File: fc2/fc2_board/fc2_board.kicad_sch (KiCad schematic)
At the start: 5 parts, among them U1 MPU-6050, U2 STM32G070RBTx

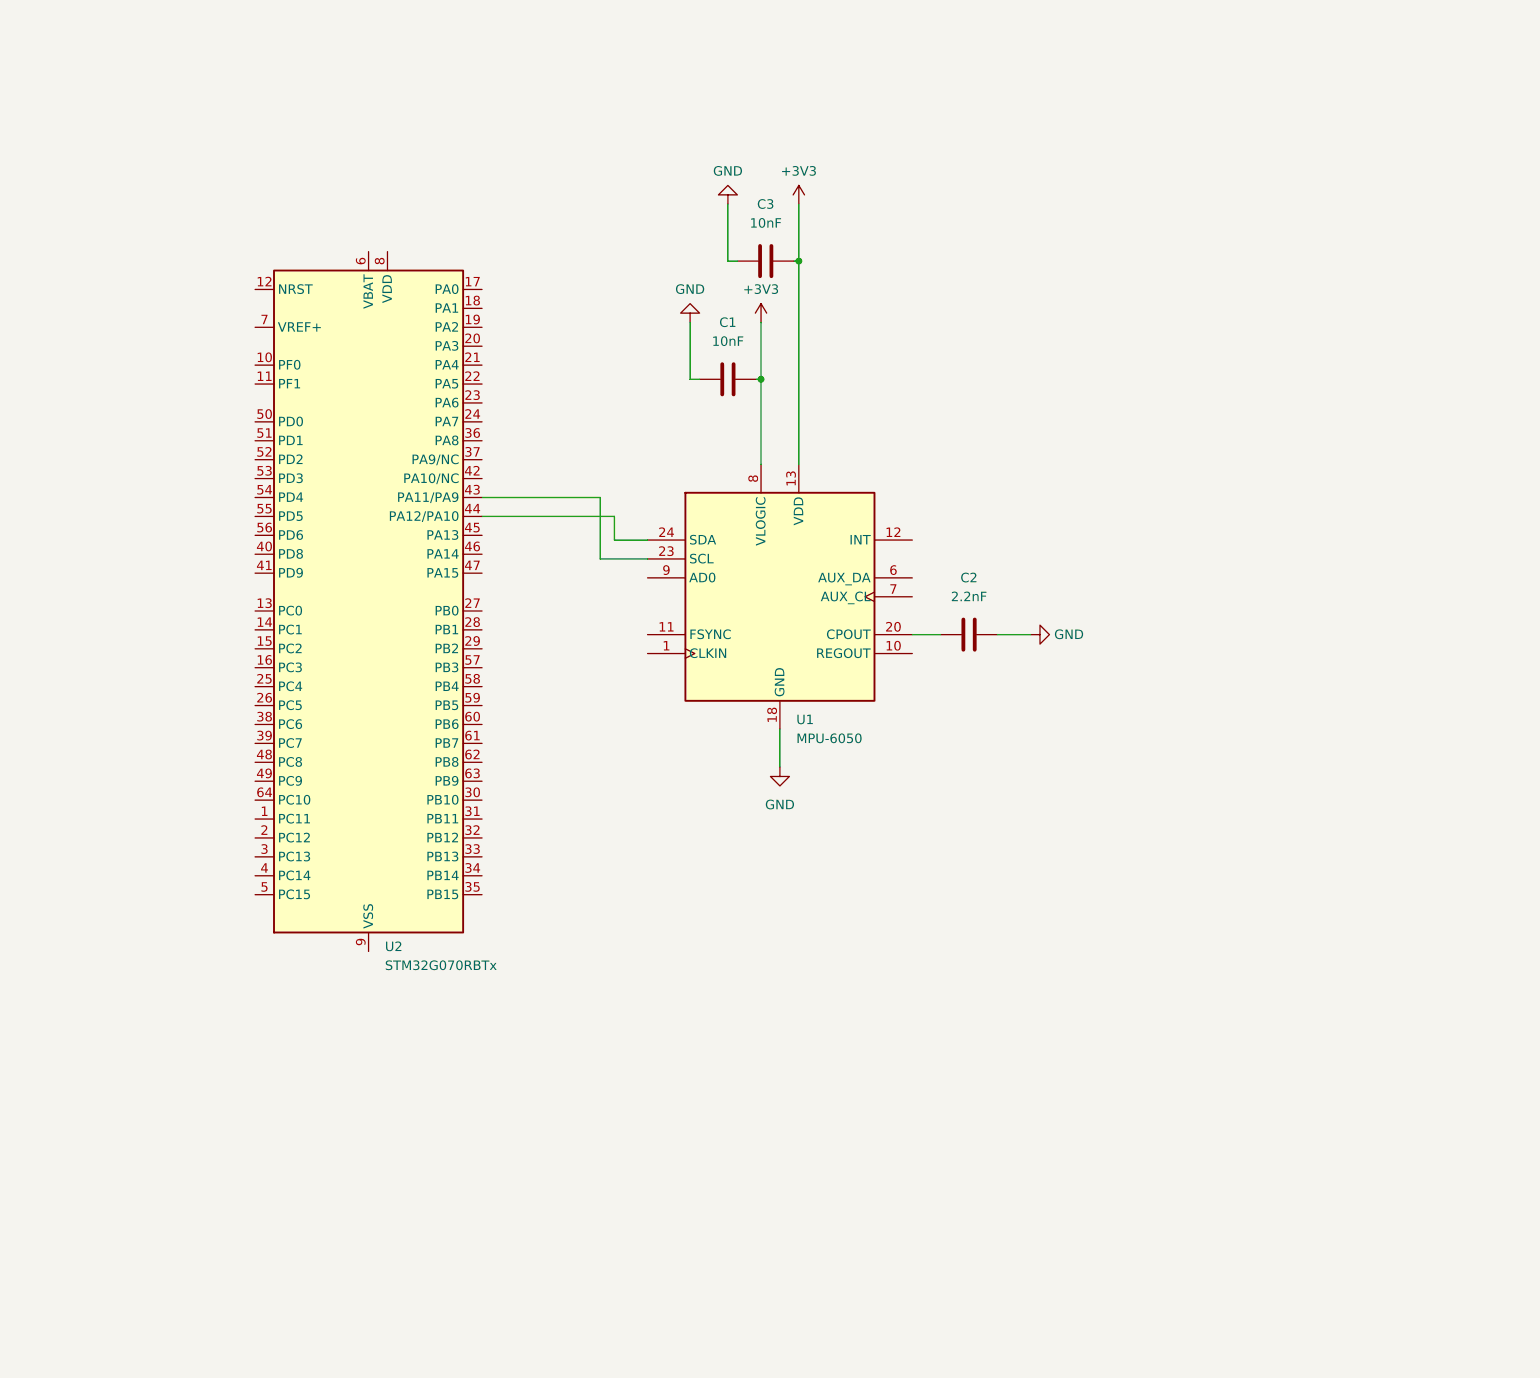
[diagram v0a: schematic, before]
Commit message: feat: add power on LED
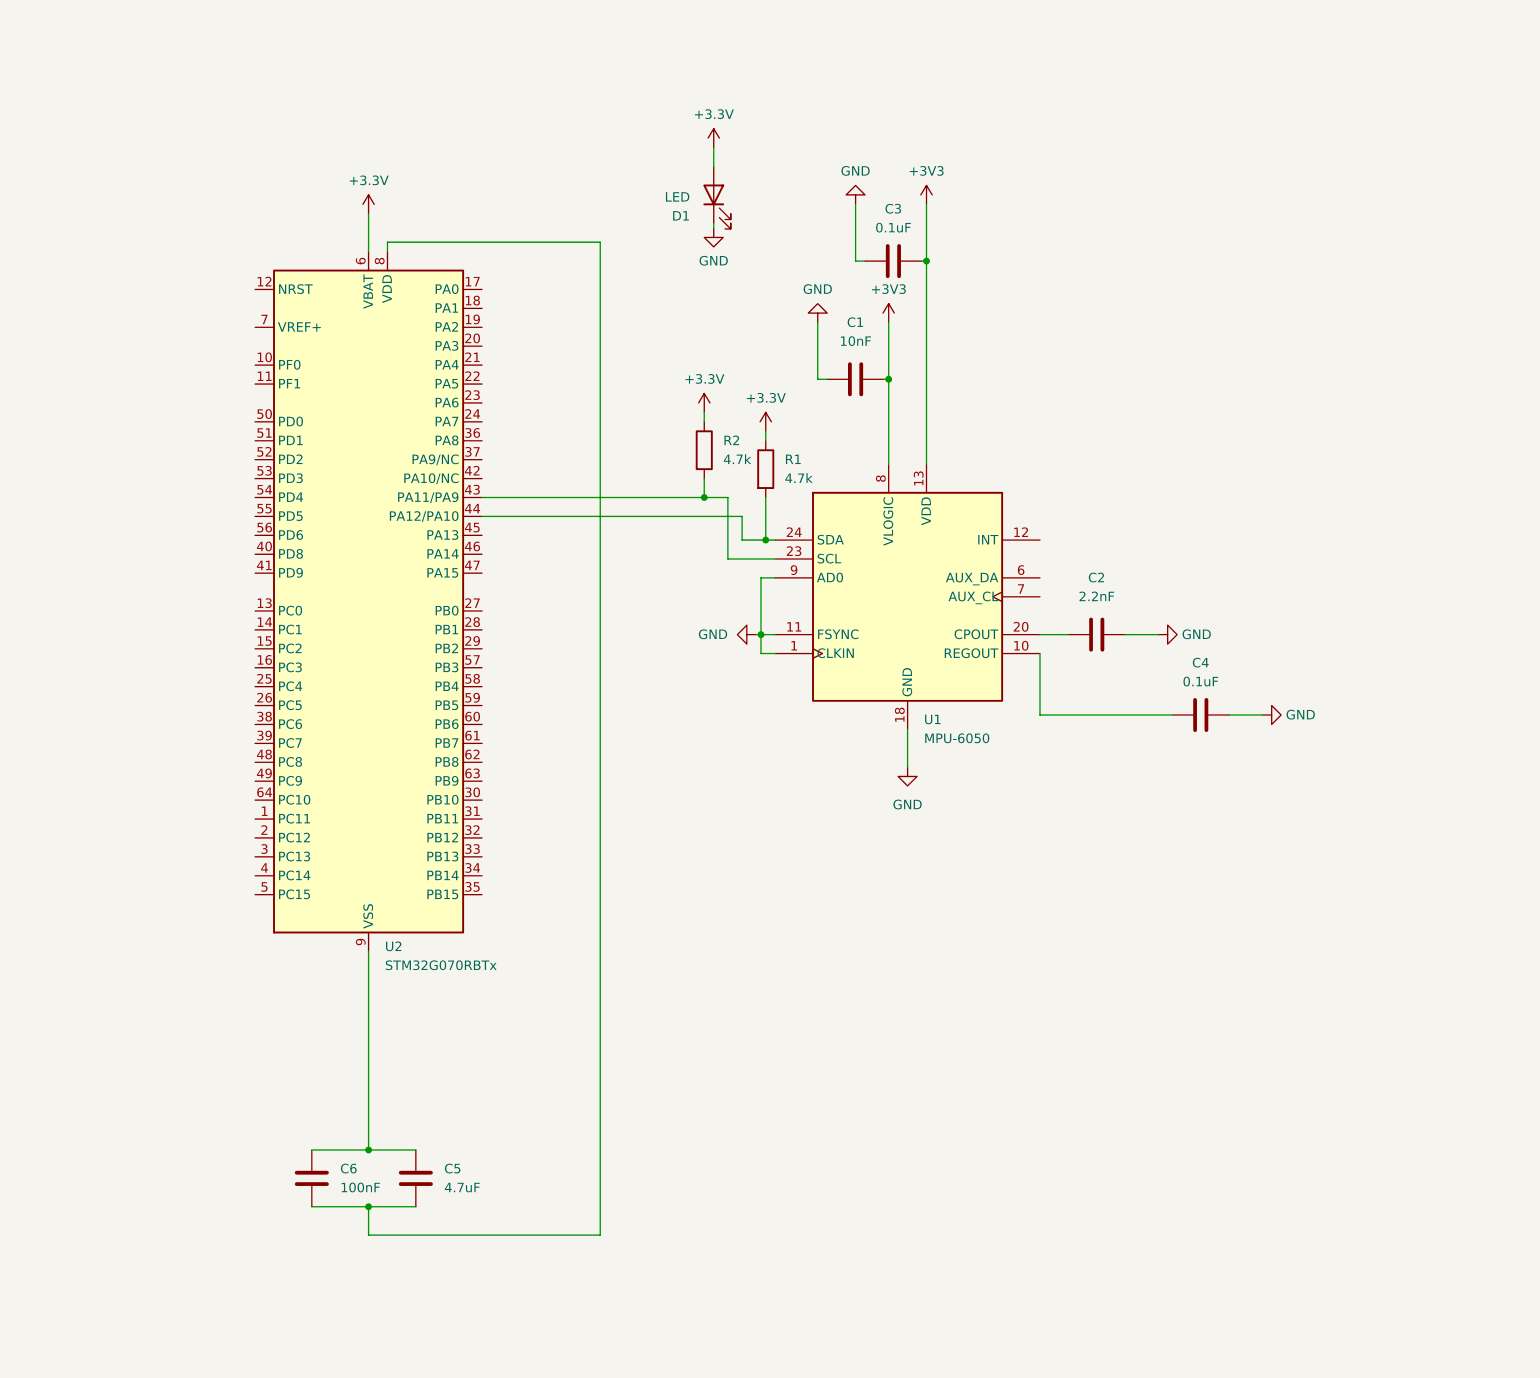
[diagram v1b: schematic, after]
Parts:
- added C4: 0.1uF, symbol Device:C
- added C5: 4.7uF, symbol Device:C
- added C6: 100nF, symbol Device:C
- added D1: LED, symbol Device:LED
- added R1, R2: 4.7k, symbol Device:R
- C3: value 10nF -> 0.1uF
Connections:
- net GND: now also U1.1 (CLKIN), U1.11 (FSYNC), U1.9 (AD0), C4.2, D1.1 (K)
- net at U1.10 (REGOUT): now also C4.1
- net at U1.23 (SCL), U2.43 (PA11/PA9): now also R2.2
- net at U1.24 (SDA), U2.44 (PA12/PA10): now also R1.2
- net +3.3V: now reaches U2.6 (VBAT)
- net +3.3V: now also D1.2 (A), R1.1, R2.1
- net at U2.8 (VDD): now also C5.2, C6.2
- net at U2.9 (VSS): now also C5.1, C6.1
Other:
- moved on the sheet: C1, C2, C3, U1

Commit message: kicad: add SAM-m10q to fc2
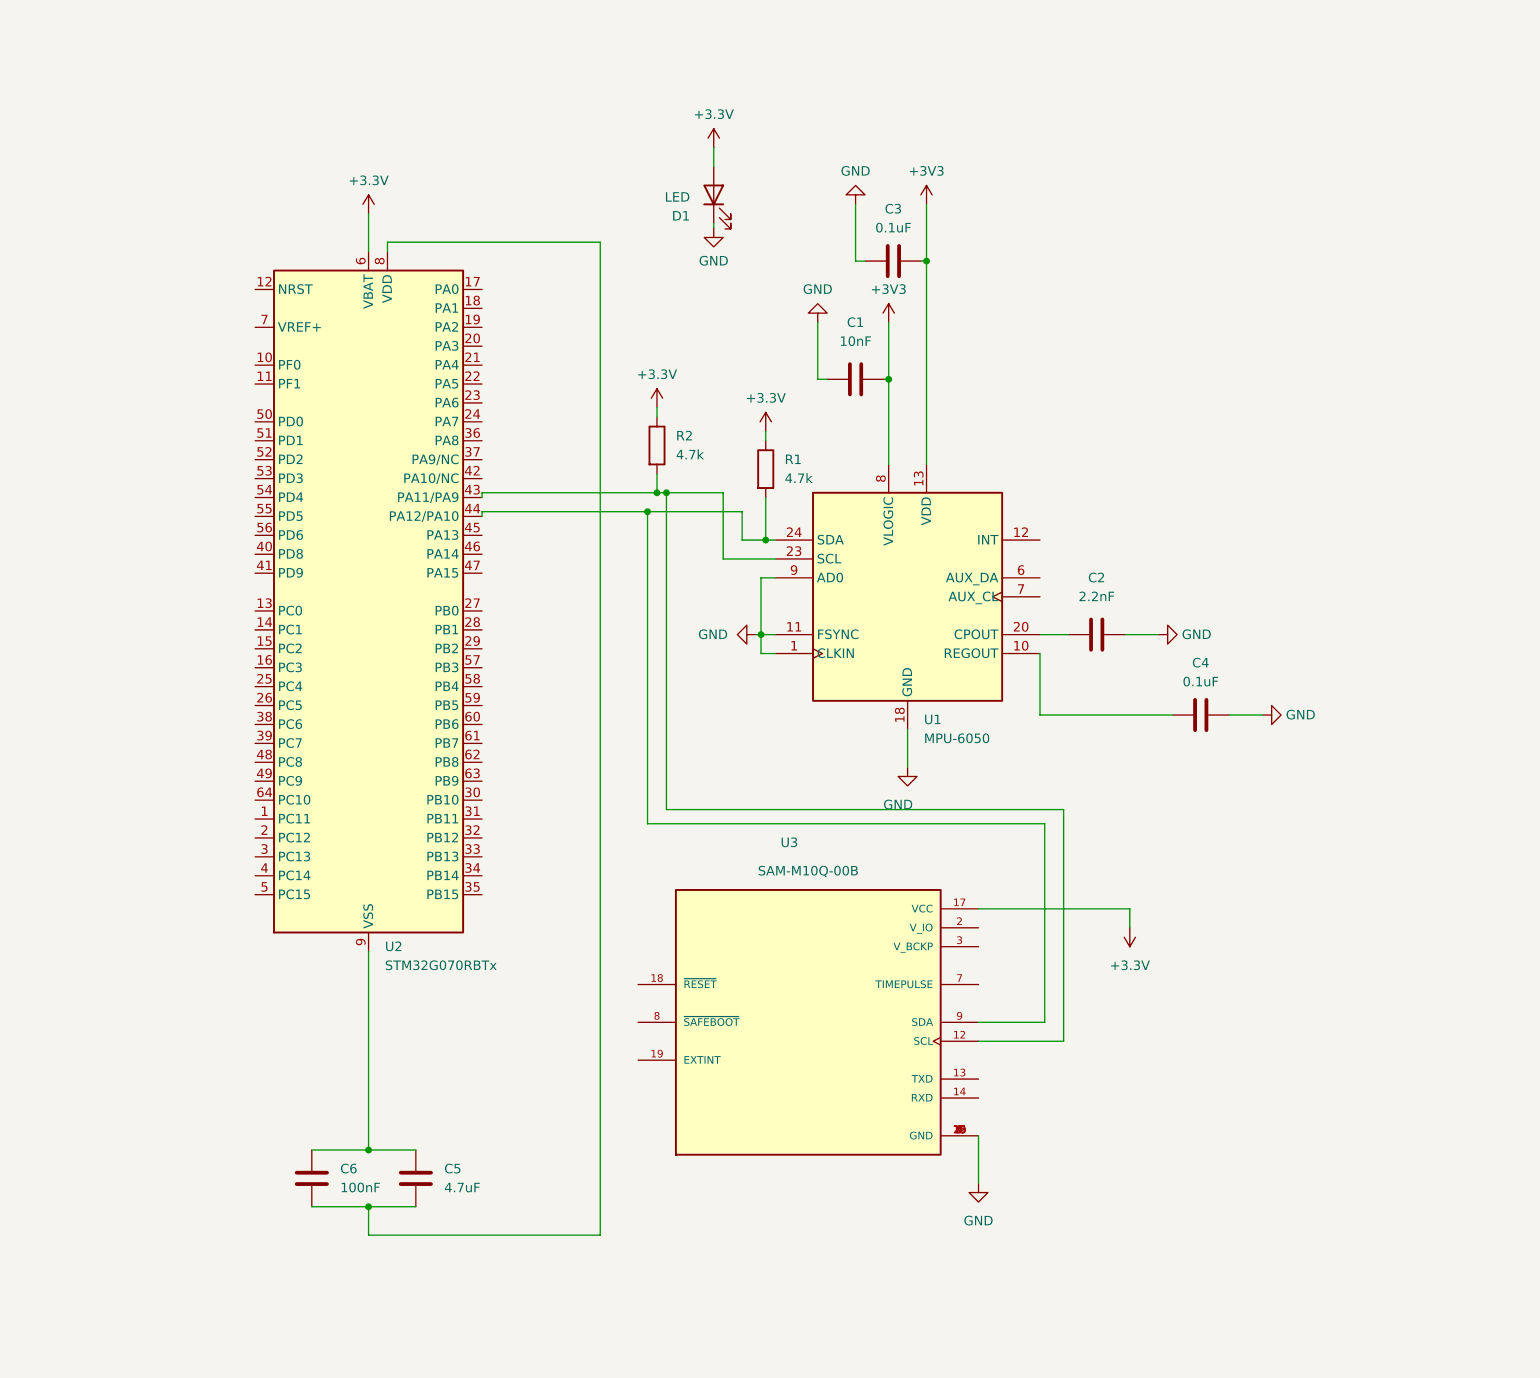
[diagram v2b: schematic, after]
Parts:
- added U3: SAM-M10Q-00B, SAM-M10Q-00B:XCVR_SAM-M10Q-00B, symbol Ext_SAM_M10Q:SAM-M10Q-00B
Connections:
- net +3.3V: now also U3.17 (VCC)
- net GND: now also U3.1 (GND), U3.10 (GND), U3.11 (GND), U3.15 (GND), U3.16 (GND), U3.20 (GND), U3.4 (GND), U3.5 (GND), U3.6 (GND)
- net at R2.2, U1.23 (SCL), U2.43 (PA11/PA9): now also U3.12 (SCL)
- net at R1.2, U1.24 (SDA), U2.44 (PA12/PA10): now also U3.9 (SDA)
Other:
- moved on the sheet: R2

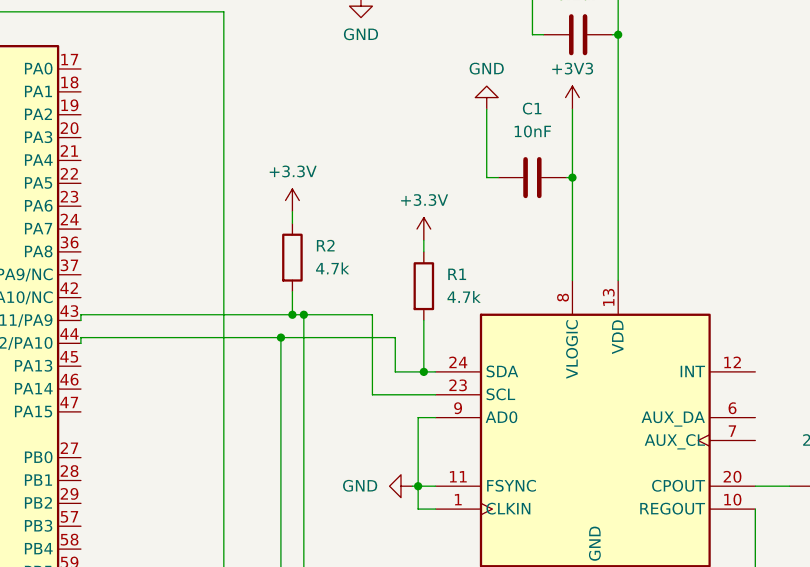
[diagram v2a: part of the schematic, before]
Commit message: feat: bump i2c1 to fast mode
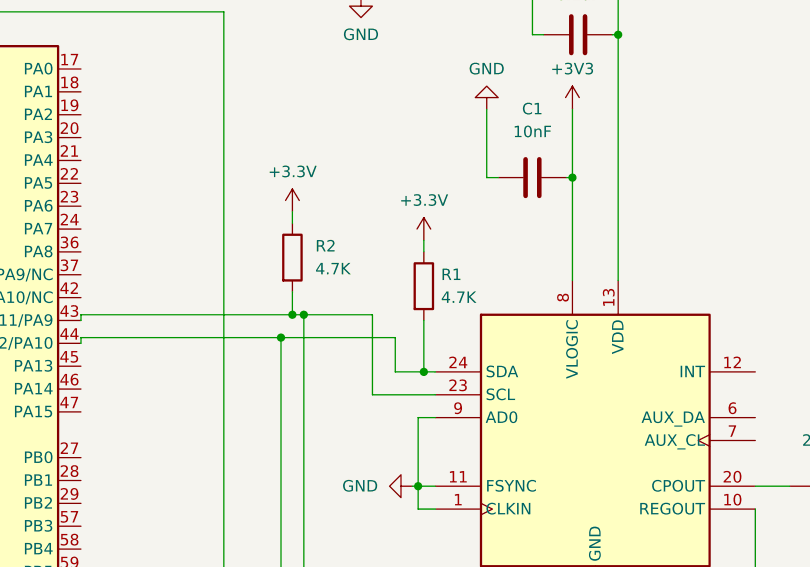
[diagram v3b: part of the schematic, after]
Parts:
- R1, R2: value 4.7k -> 4.7K
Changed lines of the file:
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@@
       (effects (font (size 1.27 1.27)) (justify left))
     )
-    (property "Value" "4.7k" (at 128.27 74.93 0)
+    (property "Value" "4.7K" (at 128.27 74.93 0)
       (effects (font (size 1.27 1.27)) (justify left))
     )
@@
   (symbol (lib_id "Device:R") (at 140.335 76.835 0) (unit 1)
     (in_bom yes) (on_board yes) (dnp no) (fields_autoplaced)
-    (property "Reference" "R1" (at 142.875 75.565 0)
-      (effects (font (size 1.27 1.27)) (justify left))
-    )
-    (property "Value" "4.7k" (at 142.875 78.105 0)
-      (effects (font (size 1.27 1.27)) (justify left))
-    )
+    (property "Reference" "R1" (at 142.24 75.565 0)
+      (effects (font (size 1.27 1.27)) (justify left))
+    )
+    (property "Value" "4.7K" (at 142.24 78.105 0)
+      (effects (font (size 1.27 1.27)) (justify left))
+    )

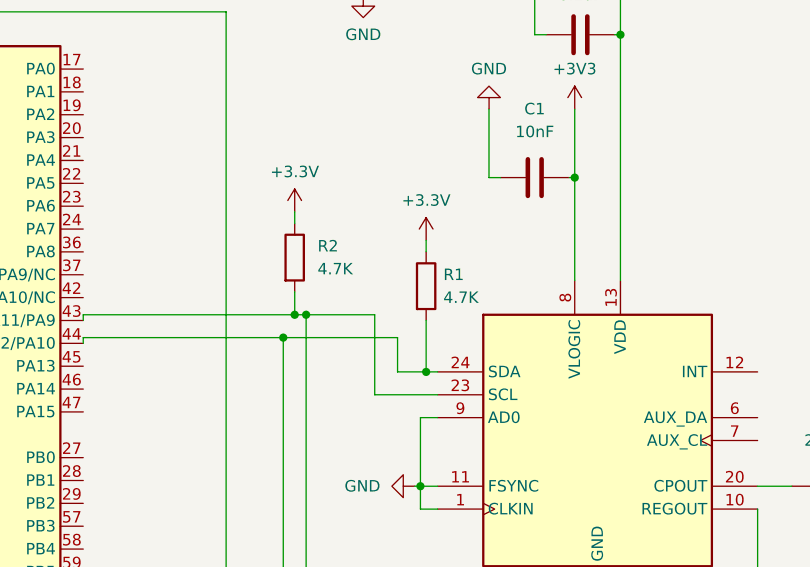
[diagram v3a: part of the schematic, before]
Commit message: fix: adjust i2c pull up resistor for extra dev
GY-521 breakout board uses a 4.7K for the MPU6050 and the Sparkfun
Breakout board for the SAM M10Q uses 2.2K.

Total Capacitance:
- MPU6050: <5pF
- STM32G070RB: 5pF
- SAM M10Q: 10pF
- Trace/Pad/Stray/Wire etc.: ??

For I2C fast at 3.3V with a conservative estimate of total 100pF bus
capacitance:

- R_pu_min is 1.1K
- R_pu_max of 3.54K

Not going to worry about power drain so just going to set R_pu at 1.5K
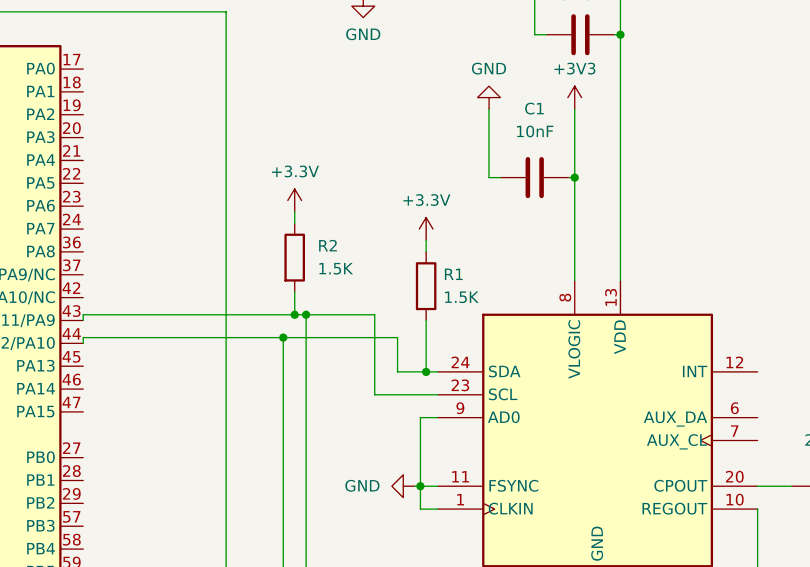
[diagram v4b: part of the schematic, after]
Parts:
- R1, R2: value 4.7K -> 1.5K
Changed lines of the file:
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@@
       (effects (font (size 1.27 1.27)) (justify left))
     )
-    (property "Value" "4.7K" (at 128.27 74.93 0)
+    (property "Value" "1.5K" (at 128.27 74.93 0)
       (effects (font (size 1.27 1.27)) (justify left))
     )
@@
       (effects (font (size 1.27 1.27)) (justify left))
     )
-    (property "Value" "4.7K" (at 142.24 78.105 0)
-      (effects (font (size 1.27 1.27)) (justify left))
-    )
+    (property "Value" "1.5K" (at 142.24 78.105 0)
+      (effects (font (size 1.27 1.27)) (justify left))
+    )
